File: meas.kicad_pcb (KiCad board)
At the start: 2 copper layers, 100 x 220 mm, 235 parts, among them J101 Conn_01x06_Socket, J102 Conn_01x02_Socket, J103 Conn_01x02_Socket, J104 Conn_01x02_Socket, J105 Conn_01x02_Socket, Q1001 DPLS350E, U1001 MC7805, U201 Si8641BD-B-IS2, U202 R05C05TE05S, U301 Si8641BD-B-IS2, U302 R05C05TE05S, U401 Si8641BD-B-IS2, U402 R05C05TE05S, U501 Si8641BD-B-IS2, U502 R05C05TE05S, U601 ADS8665IPWR, U701 ADS8665IPWR, U801 ADS8665IPWR, U901 ACS730xLCTR-20AB

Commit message: separate digital-interface and iso-dcdc
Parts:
- removed the C201 at (-105.7, 112.4)
- removed the C203 at (-111.1, 90.8)
- removed the C206 at (-105.7, 116.6)
- removed C207, C307, C407, C507: 100n, meas:C_0805_2012Metric_Pad1.18x1.45mm_HandSolder
- removed the C301 at (-107.0, 169.5)
- removed the C303 at (-112.4, 148.0)
- removed the C306 at (-107.0, 173.8)
- removed the C401 at (-103.4, 229.3)
- removed the C403 at (-108.8, 207.8)
- removed the C406 at (-103.4, 233.5)
- removed the C501 at (-106.0, 36.4)
- removed the C503 at (-111.4, 14.8)
- removed the C506 at (-106.0, 40.6)
- removed D205, D305, D405, D505: PDZ5.6B115, meas:D_SOD-323_HandSoldering
- removed the R201 at (-92.8, 88.4)
- removed the R206 at (-86.9, 88.4)
- removed the R301 at (-94.1, 145.6)
- removed the R306 at (-88.2, 145.6)
- removed the R401 at (-90.6, 205.4)
- removed the R406 at (-84.6, 205.4)
- removed the R501 at (-93.1, 12.4)
- removed the R506 at (-87.1, 12.4)
- removed the TP205 at (-93.9, 121.1)
- removed the TP206 at (-90.0, 108.9)
- removed the TP305 at (-95.2, 178.2)
- removed the TP306 at (-91.3, 166.1)
- removed the TP405 at (-91.6, 238.0)
- removed the TP406 at (-87.8, 225.8)
- removed the TP505 at (-94.1, 45.1)
- removed the TP506 at (-90.3, 32.9)
- removed U202, U302, U402, U502: R05C05TE05S, meas:SOIC-16W_7.5x10.3mm_P1.27mm
- added C1101: 10u, meas:C_1210_3225Metric_Pad1.33x2.70mm_HandSolder, F.Cu at (115.7, 120.2)
- added C1102: 100n, meas:C_0805_2012Metric_Pad1.18x1.45mm_HandSolder, F.Cu at (120.1, 112.6)
- added C1103: 10u, meas:C_1210_3225Metric_Pad1.33x2.70mm_HandSolder, F.Cu at (109.3, 120.2)
- added C1104: 100n, meas:C_0805_2012Metric_Pad1.18x1.45mm_HandSolder, F.Cu at (104.9, 112.6)
- added C1201: 10u, meas:C_1210_3225Metric_Pad1.33x2.70mm_HandSolder, F.Cu at (116.3, 174.1)
- added C1202: 100n, meas:C_0805_2012Metric_Pad1.18x1.45mm_HandSolder, F.Cu at (120.8, 166.5)
- added C1203: 10u, meas:C_1210_3225Metric_Pad1.33x2.70mm_HandSolder, F.Cu at (110.0, 174.1)
- added C1204: 100n, meas:C_0805_2012Metric_Pad1.18x1.45mm_HandSolder, F.Cu at (105.5, 166.5)
- added C1301: 10u, meas:C_1210_3225Metric_Pad1.33x2.70mm_HandSolder, F.Cu at (116.3, 219.9)
- added C1302: 100n, meas:C_0805_2012Metric_Pad1.18x1.45mm_HandSolder, F.Cu at (120.8, 212.2)
- added C1303: 10u, meas:C_1210_3225Metric_Pad1.33x2.70mm_HandSolder, F.Cu at (110.0, 219.9)
- added C1304: 100n, meas:C_0805_2012Metric_Pad1.18x1.45mm_HandSolder, F.Cu at (105.5, 212.2)
- added C1401: 10u, meas:C_1210_3225Metric_Pad1.33x2.70mm_HandSolder, F.Cu at (170.2, 82.2)
- added C1402: 100n, meas:C_0805_2012Metric_Pad1.18x1.45mm_HandSolder, F.Cu at (162.5, 77.8)
- added C1403: 10u, meas:C_1210_3225Metric_Pad1.33x2.70mm_HandSolder, F.Cu at (170.2, 88.5)
- added C1404: 100n, meas:C_0805_2012Metric_Pad1.18x1.45mm_HandSolder, F.Cu at (162.5, 93.0)
- added D1101: PDZ5.6B115, meas:D_SOD-323_HandSoldering, F.Cu at (122.7, 112.6)
- added D1201: PDZ5.6B115, meas:D_SOD-323_HandSoldering, F.Cu at (123.3, 166.5)
- added D1301: PDZ5.6B115, meas:D_SOD-323_HandSoldering, F.Cu at (123.3, 212.2)
- added D1401: PDZ5.6B115, meas:D_SOD-323_HandSoldering, F.Cu at (162.5, 75.2)
- added R1101: 330, meas:R_1210_3225Metric_Pad1.30x2.65mm_HandSolder, F.Cu at (120.1, 105.6)
- added R1102: 1M, meas:R_1210_3225Metric_Pad1.30x2.65mm_HandSolder, F.Cu at (112.5, 105.6)
- added R1201: 330, meas:R_1210_3225Metric_Pad1.30x2.65mm_HandSolder, F.Cu at (120.8, 159.5)
- added R1202: 1M, meas:R_1210_3225Metric_Pad1.30x2.65mm_HandSolder, F.Cu at (113.1, 159.5)
- added R1301: 330, meas:R_1210_3225Metric_Pad1.30x2.65mm_HandSolder, F.Cu at (120.8, 205.3)
- added R1302: 1M, meas:R_1210_3225Metric_Pad1.30x2.65mm_HandSolder, F.Cu at (113.1, 205.3)
- added R1401: 330, meas:R_1210_3225Metric_Pad1.30x2.65mm_HandSolder, F.Cu at (155.5, 77.8)
- added R1402: 1M, meas:R_1210_3225Metric_Pad1.30x2.65mm_HandSolder, F.Cu at (155.6, 85.4)
- added TP1101: ~, meas:TP_0805_2012Metric, F.Cu at (116.3, 105.6)
- added TP1102: ~, meas:TP_0805_2012Metric, F.Cu at (123.9, 105.6)
- added TP1201: ~, meas:TP_0805_2012Metric, F.Cu at (116.9, 159.5)
- added TP1202: ~, meas:TP_0805_2012Metric, F.Cu at (124.6, 159.5)
- added TP1301: ~, meas:TP_0805_2012Metric, F.Cu at (116.9, 205.3)
- added TP1302: ~, meas:TP_0805_2012Metric, F.Cu at (124.6, 205.3)
- added TP1401: ~, meas:TP_0805_2012Metric, F.Cu at (155.6, 81.6)
- added TP1402: ~, meas:TP_0805_2012Metric, F.Cu at (155.5, 73.9)
- added U1101: R05C05TE05S, meas:SOIC-16W_7.5x10.3mm_P1.27mm, F.Cu at (112.5, 112.6)
- added U1201: R05C05TE05S, meas:SOIC-16W_7.5x10.3mm_P1.27mm, F.Cu at (113.1, 166.5)
- added U1301: R05C05TE05S, meas:SOIC-16W_7.5x10.3mm_P1.27mm, F.Cu at (113.1, 212.2)
- added U1401: R05C05TE05S, meas:SOIC-16W_7.5x10.3mm_P1.27mm, F.Cu at (162.5, 85.4)
- moved C503 310.7 mm to (191.7, 88.9), turned to 90 degrees
- moved C502 309.8 mm to (191.7, 81.8), turned to -90 degrees
- moved C504 308.8 mm to (189.6, 96.0), turned to -90 degrees
- moved C505 302.6 mm to (183.9, 96.0), turned to -90 degrees
- moved C506 296.3 mm to (178.2, 96.0), turned to -90 degrees
- moved C501 295.9 mm to (177.6, 75.4), turned to 90 degrees
- moved U501 295.5 mm to (184.8, 85.4), turned to -90 degrees
- moved R501 291.5 mm to (192.4, 75.8), turned to -90 degrees
- moved TP505 289.7 mm to (192.4, 99.3)
- moved R506 289.3 mm to (192.4, 95.5), turned to -90 degrees
- moved TP501 289.2 mm to (192.4, 72.0), turned to 180 degrees
- moved R502 287.0 mm to (188.6, 75.8), turned to -90 degrees
- moved TP502 285.0 mm to (188.6, 72.0), turned to 180 degrees
- moved TP506 283.5 mm to (186.7, 99.3)
- moved R507 282.7 mm to (186.7, 95.5), turned to -90 degrees
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- renumbered C202 to C201, C204 to C202, C205 to C203, C208 to C204, C209 to C205, C210 to C206, C302 to C301, C304 to C302, C305 to C303, C308 to C304, C309 to C305, C310 to C306, C402 to C401, C404 to C402, C405 to C403, C408 to C404, C409 to C405, C410 to C406, C502 to C501, C504 to C502, C505 to C503, C508 to C504, C509 to C505, C510 to C506, R202 to R201, R203 to R202, R204 to R203, R205 to R204, R207 to R205, R208 to R206, R209 to R207, R210 to R208, R302 to R301, R303 to R302, R304 to R303, R305 to R304, R307 to R305, R308 to R306, R309 to R307, R310 to R308, R402 to R401, R403 to R402, R404 to R403, R405 to R404, R407 to R405, R408 to R406, R409 to R407, R410 to R408, R502 to R501, R503 to R502, R504 to R503, R505 to R504, R507 to R505, R508 to R506, R509 to R507, R510 to R508, TP207 to TP205, TP208 to TP206, TP209 to TP207, TP210 to TP208, TP307 to TP305, TP308 to TP306, TP309 to TP307, TP310 to TP308, TP407 to TP405, TP408 to TP406, TP409 to TP407, TP410 to TP408, TP507 to TP505, TP508 to TP506, TP509 to TP507, TP510 to TP508
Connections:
- net /digital-interface3/+5VA_ISO renamed /digital-interface3/+5VA_MASTER
- net /digital-interface3/GND_ISO renamed /digital-interface3/GND_MASTER
- C701 pad 1: /GND_ISO_I -> /adc1/GND_ADC
- C702 pad 1: /GND_ISO_I -> /adc1/GND_ADC
- C703 pad 1: /GND_ISO_I -> /adc1/GND_ADC
- C705 pad 1: /GND_ISO_I -> /adc1/GND_ADC
- C706 pad 1: /GND_ISO_I -> /adc1/GND_ADC
- C707 pad 1: /GND_ISO_I -> /adc1/GND_ADC
- C801 pad 1: /GND_ISO_T -> /adc2/GND_ADC
- C802 pad 1: /GND_ISO_T -> /adc2/GND_ADC
- C802 pad 2: /+5VA_ISO_T -> /adc2/+5VA_ADC
- C803 pad 1: /GND_ISO_T -> /adc2/GND_ADC
- C803 pad 2: /+5VA_ISO_T -> /adc2/+5VA_ADC
- C805 pad 1: /GND_ISO_T -> /adc2/GND_ADC
- C806 pad 1: /GND_ISO_T -> /adc2/GND_ADC
- C807 pad 1: /GND_ISO_T -> /adc2/GND_ADC
- D701 pad 1: /GND_ISO_I -> /adc1/GND_ADC
- D801 pad 1: /GND_ISO_T -> /adc2/GND_ADC
- JP801 pad 1: /+5VA_ISO_T -> /adc2/+5VA_ADC
- R704 pad 2: /GND_ISO_I -> /adc1/GND_ADC
- R801 pad 1: /+5VA_ISO_T -> /adc2/+5VA_ADC
- R804 pad 2: /GND_ISO_T -> /adc2/GND_ADC
- U701 pad 1: /GND_ISO_I -> /adc1/GND_ADC
- U701 pad 3: /GND_ISO_I -> /adc1/GND_ADC
- U701 pad 5: /GND_ISO_I -> /adc1/GND_ADC
- U801 pad 1: /GND_ISO_T -> /adc2/GND_ADC
- U801 pad 16: /+5VA_ISO_T -> /adc2/+5VA_ADC
- U801 pad 2: /+5VA_ISO_T -> /adc2/+5VA_ADC
- U801 pad 3: /GND_ISO_T -> /adc2/GND_ADC
- U801 pad 5: /GND_ISO_T -> /adc2/GND_ADC
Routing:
- net GND: track 0.00 -> 227.2 mm, vias 0 -> 30
- net +5VA: track 0.00 -> 158.6 mm
- net /GND_ISO_U: track 43.0 -> 116.4 mm, vias 2 -> 8
- net /adc1/GND_ADC: track 0.00 -> 62.7 mm, vias 0 -> 5
- net /adc2/GND_ADC: track 0.00 -> 62.7 mm, vias 0 -> 5
- net /digital-interface3/GND_MASTER: track 0.00 -> 59.7 mm, vias 0 -> 8
- net /adc2/+5VA_ADC: track 0.00 -> 56.2 mm, vias 0 -> 2
- net /~{CS}: track 0.00 -> 52.1 mm
- net /+5VA_ISO_U: track 23.7 -> 73.8 mm
- net /+5VA_ISO_I: track 23.7 -> 73.8 mm
- net /digital-interface3/+5VA_MASTER: track 0.00 -> 49.7 mm
- net /SCKL: track 0.00 -> 44.7 mm
- net /SDO: track 0.00 -> 25.0 mm
- net /adc2/SDO-0: track 0.00 -> 19.4 mm
- net /adc1/SDO-0: track 0.00 -> 19.4 mm
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- added copper zone on F.Cu, net +5VA
- added copper zone on F.Cu, net /+5VA_ISO_I
- added copper zone on F.Cu, net /+5VA_ISO_T
- added copper zone on F.Cu, net /+5VA_ISO_U
- added copper zone on B.Cu, net /GND_ISO_I
- added copper zone on B.Cu, net /GND_ISO_T
- added copper zone on B.Cu, net /GND_ISO_U
- added copper zone on B.Cu, net /adc1/GND_ADC
- added copper zone on F.Cu, net /adc1/GND_ADC
- added copper zone on F.Cu, net /adc2/+5VA_ADC
- added copper zone on B.Cu, net /adc2/GND_ADC
- added copper zone on F.Cu, net /adc2/GND_ADC
- added copper zone on F.Cu, net /digital-interface3/+5VA_MASTER
- added copper zone on B.Cu, net /digital-interface3/GND_MASTER
- added copper zone on F.Cu, net /digital-interface3/GND_MASTER
- added copper zone on B.Cu, net GND
- added copper zone on F.Cu, net GND
- added copper zone on F.Cu, net Net-(U601-REFCAP)
- added copper zone on F.Cu, net Net-(U701-REFCAP)

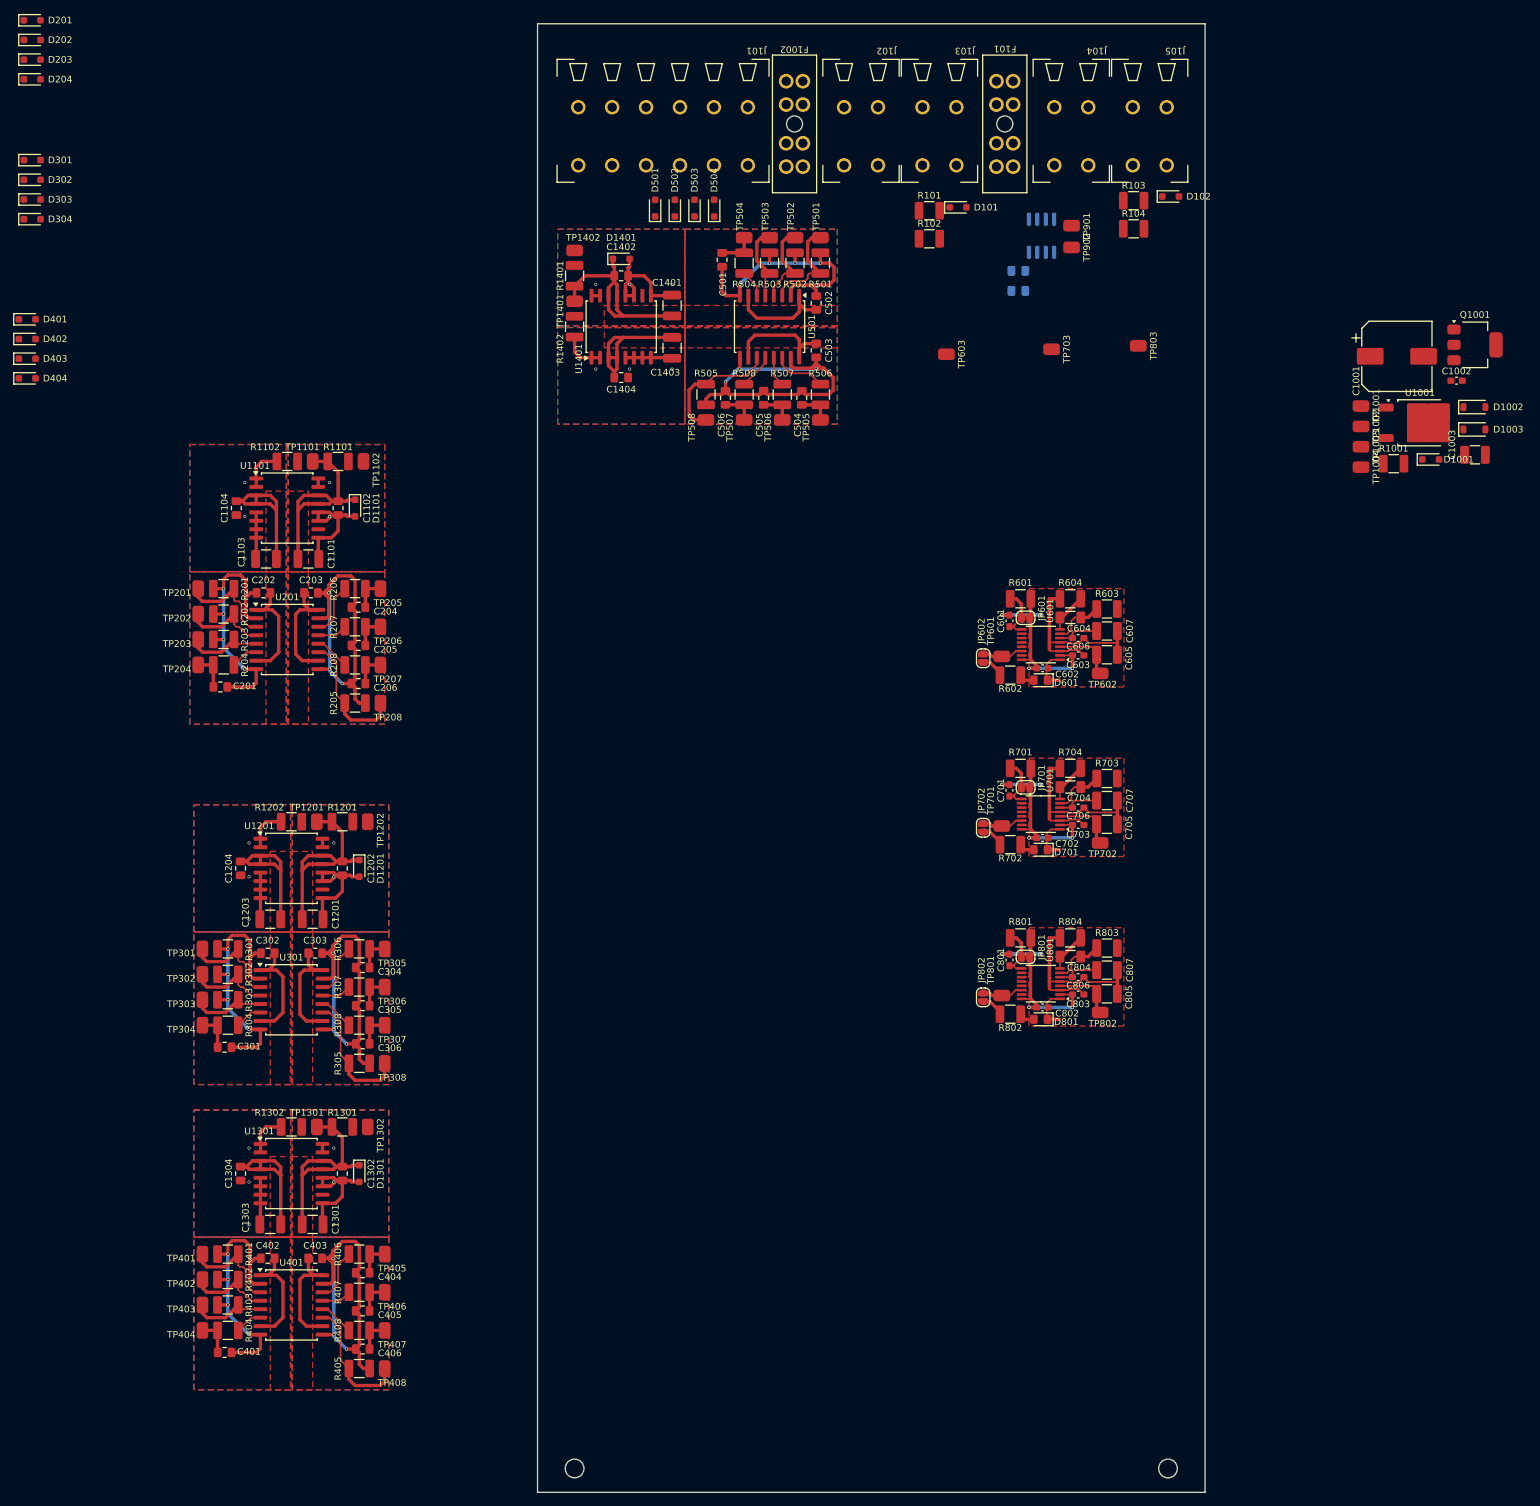
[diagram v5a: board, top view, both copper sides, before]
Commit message: add interconnect layout
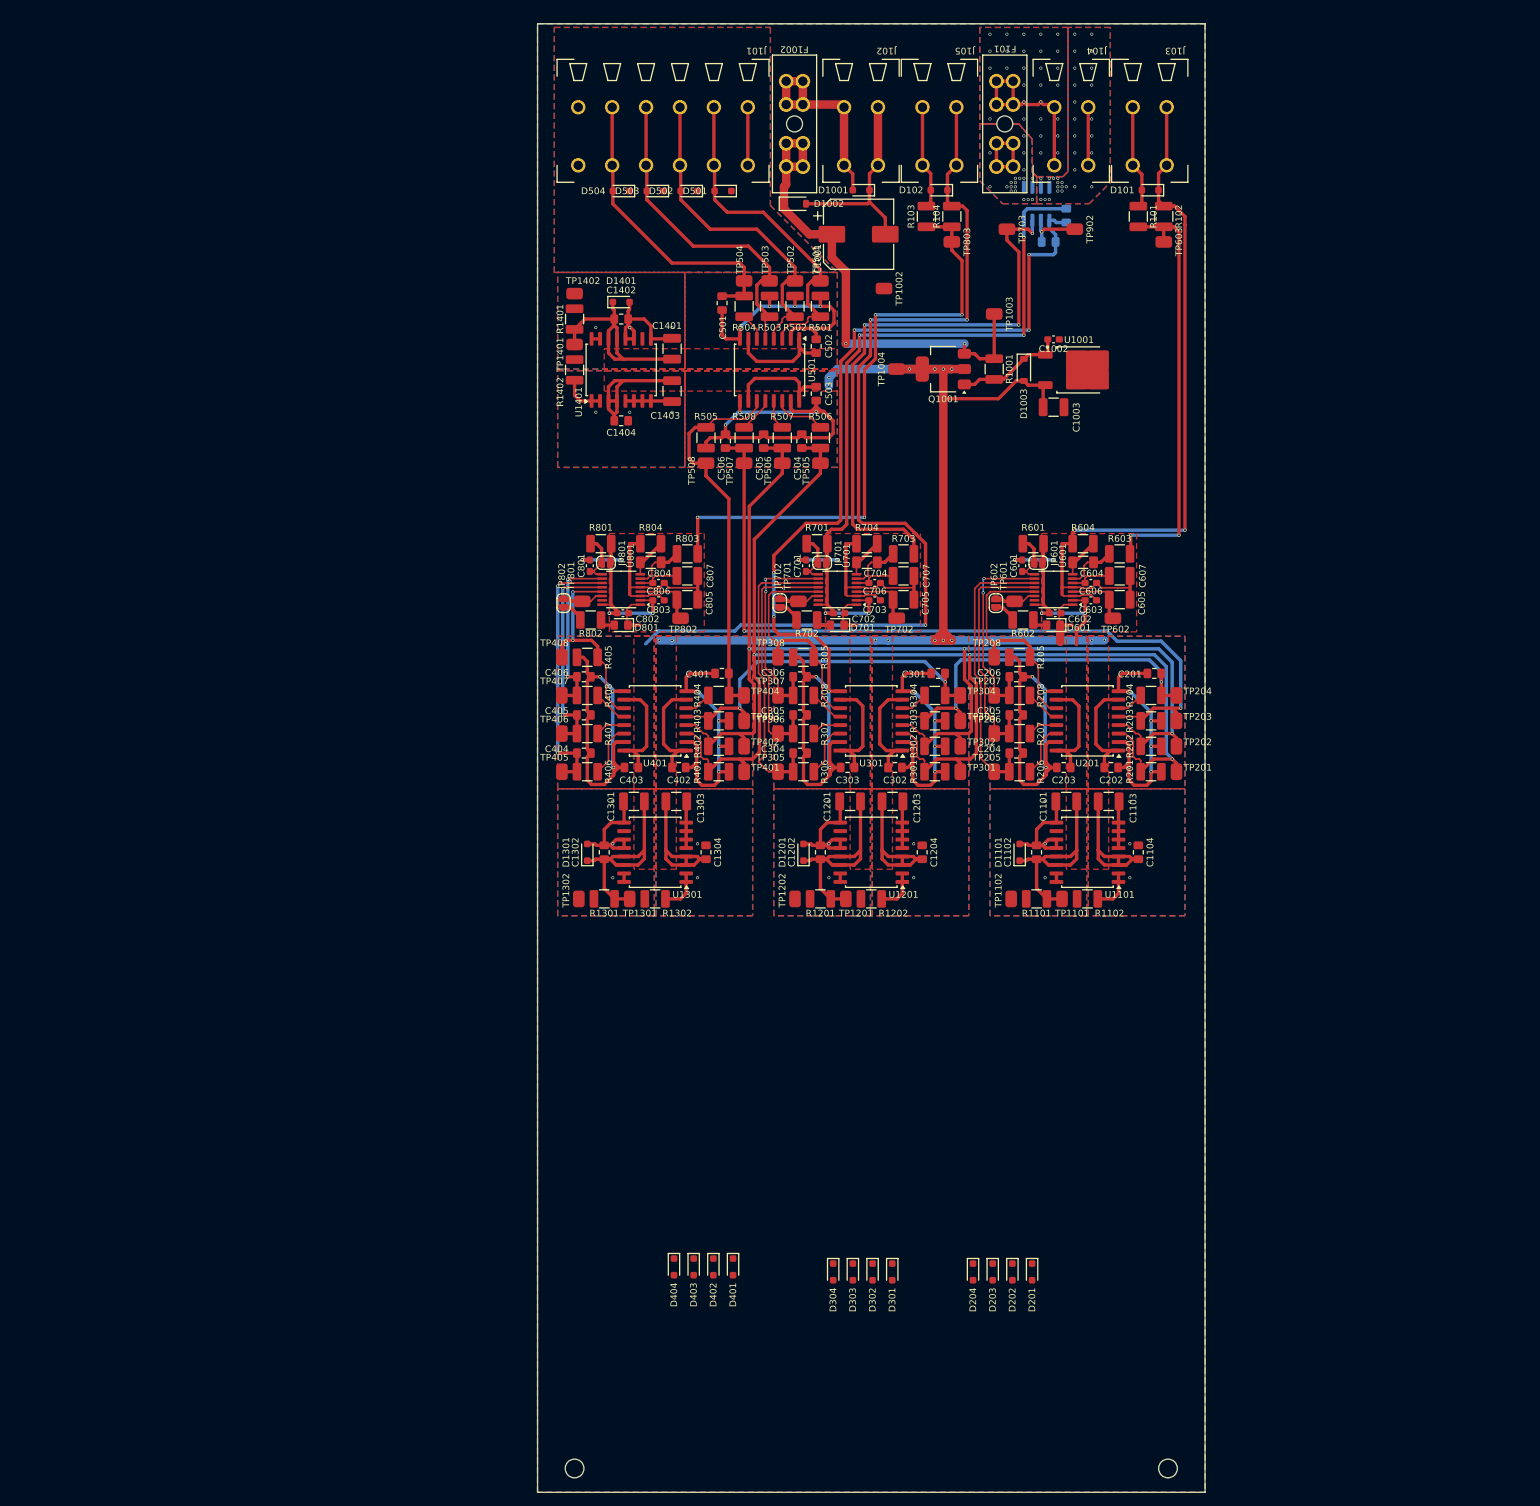
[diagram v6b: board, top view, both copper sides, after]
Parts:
- removed TP1001, TP901: ~, meas:TP_0805_2012Metric
- moved D201 240.0 mm to (224.1, 227.0), turned to -90 degrees
- moved D202 235.9 mm to (221.1, 227.0), turned to -90 degrees
- moved D203 231.7 mm to (218.2, 227.0), turned to -90 degrees
- moved D204 227.6 mm to (215.2, 227.0), turned to -90 degrees
- moved D301 210.6 mm to (203.1, 227.0), turned to -90 degrees
- moved D302 206.4 mm to (200.2, 227.0), turned to -90 degrees
- moved D303 202.3 mm to (197.2, 227.0), turned to -90 degrees
- moved D304 198.2 mm to (194.3, 227.0), turned to -90 degrees
- moved D401 177.0 mm to (179.3, 226.2), turned to -90 degrees
- moved D402 172.9 mm to (176.3, 226.2), turned to -90 degrees
- moved D403 168.8 mm to (173.4, 226.2), turned to -90 degrees
- moved D404 164.6 mm to (170.4, 226.2), turned to -90 degrees
- moved TP201 149.1 mm to (245.7, 152.1), turned to 90 degrees
- moved TP202 147.9 mm to (245.7, 148.2), turned to 90 degrees
- moved TP203 147.1 mm to (245.7, 144.4), turned to 90 degrees
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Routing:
- net +5VA: track 158.6 -> 322.5 mm, vias 0 -> 15
- net /GND_ISO_T: track 53.6 -> 200.1 mm, vias 3 -> 6
- net /~{CS}: track 52.1 -> 198.4 mm, vias 0 -> 3
- net /SCKL: track 44.7 -> 179.7 mm, vias 0 -> 3
- net /GND_ISO_I: track 53.6 -> 171.5 mm, vias 3 -> 8
- net /SDI: track 16.3 -> 117.1 mm, vias 0 -> 2
- net /adc2/AIN_P: track 0.00 -> 92.0 mm, vias 0 -> 4
- net /GND_ISO_U: track 116.4 -> 204.1 mm, vias 8 -> 10
- net /adc1/AIN_P: track 0.00 -> 87.1 mm, vias 0 -> 3
- net /+5VA_ISO_I: track 73.8 -> 157.6 mm, vias 2 -> 5
- net +24V: track 0.00 -> 75.2 mm, vias 0 -> 2
- net /adc/AIN_P: track 0.00 -> 64.2 mm, vias 0 -> 2
- net /digital-interface3/SDO_MASTER: track 5.57 -> 45.7 mm
- net /SDIO1: track 16.8 -> 56.6 mm, vias 0 -> 2
- net /adc1/CONVST/~{CS}: track 5.06 -> 44.8 mm
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- added copper zone on B.Cu, net +5VA
- added copper zone on B.Cu, net /+5VA_ISO_I
- added copper zone on B.Cu, net /+5VA_ISO_U
- added copper zone on B.Cu, net /adc1/SDI
- added copper zone on F.Cu, net /adc1/SDI
- added copper zone on B.Cu, net /i-transduce/in
- added copper zone on F.Cu, net /i-transduce/in
- added copper zone on B.Cu, net /i-transduce/out
- added copper zone on F.Cu, net /i-transduce/out
- added copper zone on B.Cu, net Net-(J104-Pin_2)
- added copper zone on F.Cu, net Net-(J104-Pin_2)
- removed copper zone on B.Cu, net /GND_ISO_I
- removed copper zone on F.Cu, net /GND_ISO_I
- removed copper zone on F.Cu, net Net-(U601-REFCAP)
